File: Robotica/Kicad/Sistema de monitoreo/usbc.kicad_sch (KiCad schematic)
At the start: 9 parts, among them J3 USB_C_Receptacle_USB2.0_16P, U2 USBLC6-2SC6

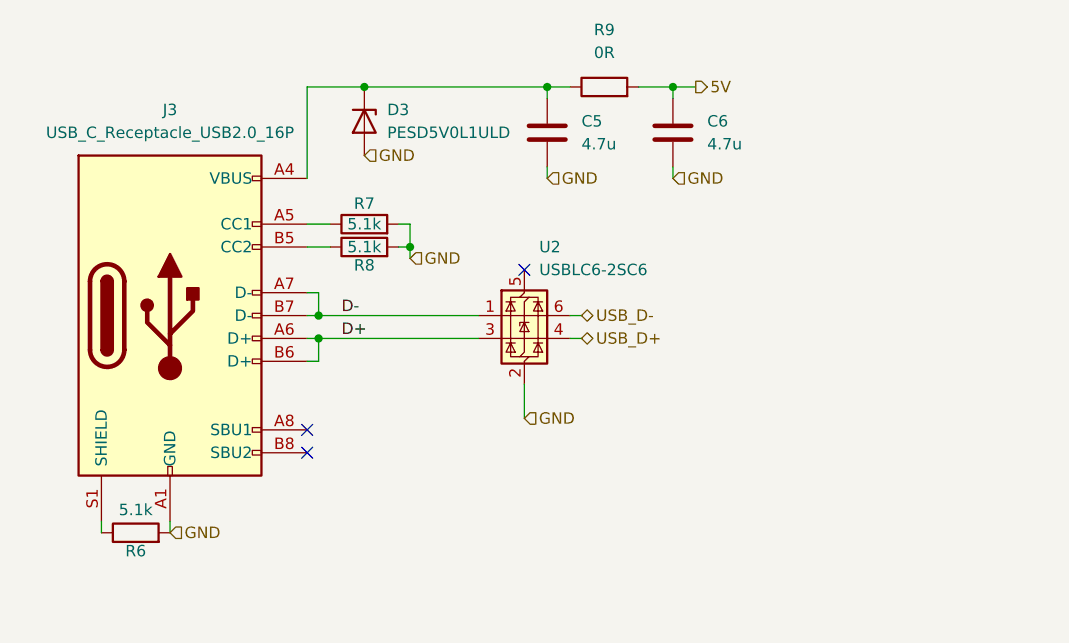
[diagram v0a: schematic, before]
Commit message: Organizacion de esquematicos de robotica
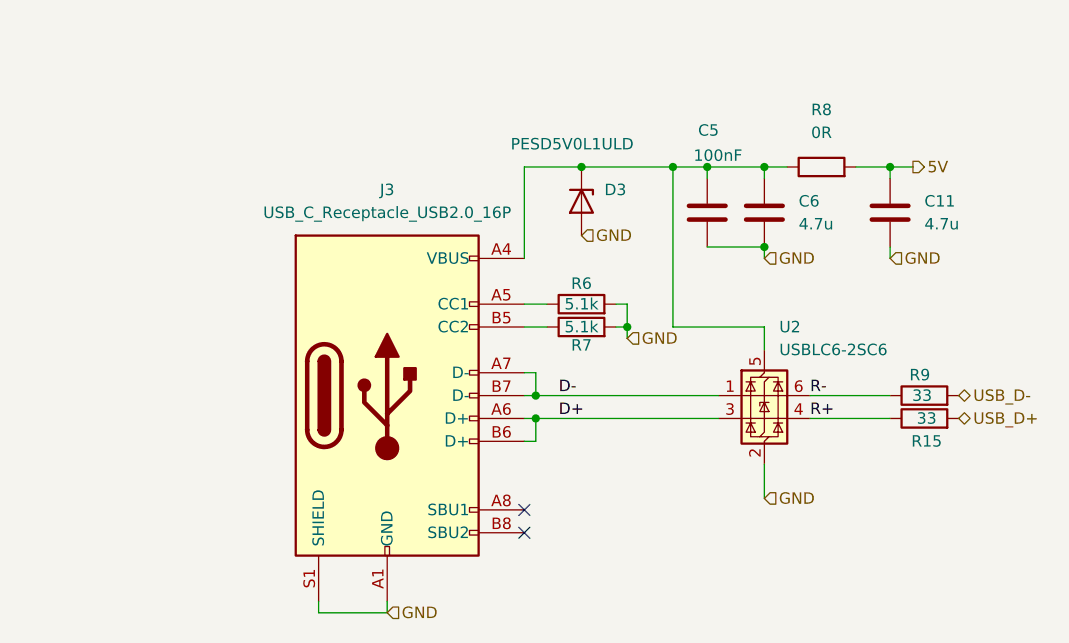
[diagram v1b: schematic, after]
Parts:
- removed R6: 5.1k, Resistor_SMD:R_0805_2012Metric_Pad1.20x1.40mm_HandSolder, symbol Device:R
- added C5: 100nF, Capacitor_SMD:C_0805_2012Metric, symbol Device:C
- added R15, R9: 33, Resistor_SMD:R_0805_2012Metric, symbol Device:R
- renumbered C6 to C11, C5 to C6, R7 to R6, R8 to R7, R9 to R8
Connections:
- net GND: now also J3.S1 (SHIELD), C5.2
- net USB_D+: now also R15.2; no longer U2.4 (I/O2)
- net USB_D-: now also R9.2; no longer U2.6 (I/O1)
- net at C6.1, D3.1 (K), J3.A4 (VBUS)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: now also U2.5 (VBUS), C5.1
- new net R+: R15.1, U2.4 (I/O2)
- new net R-: R9.1, U2.6 (I/O1)
- no-connect marks 3 -> 2
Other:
- moved on the sheet: C11, C6, D3, J3, R6, R7, R8, U2
